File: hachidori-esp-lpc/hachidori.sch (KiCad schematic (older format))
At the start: 53 parts, among them P1 VIN, P2 UART, P3 ADC, P4 I2C, SW1 FLASH, SW2 RESET, U1 NCP1117ST33, U2 MPU-9250, U3 ESP-13-WROOM-02, U4 BME280, U7 INA226

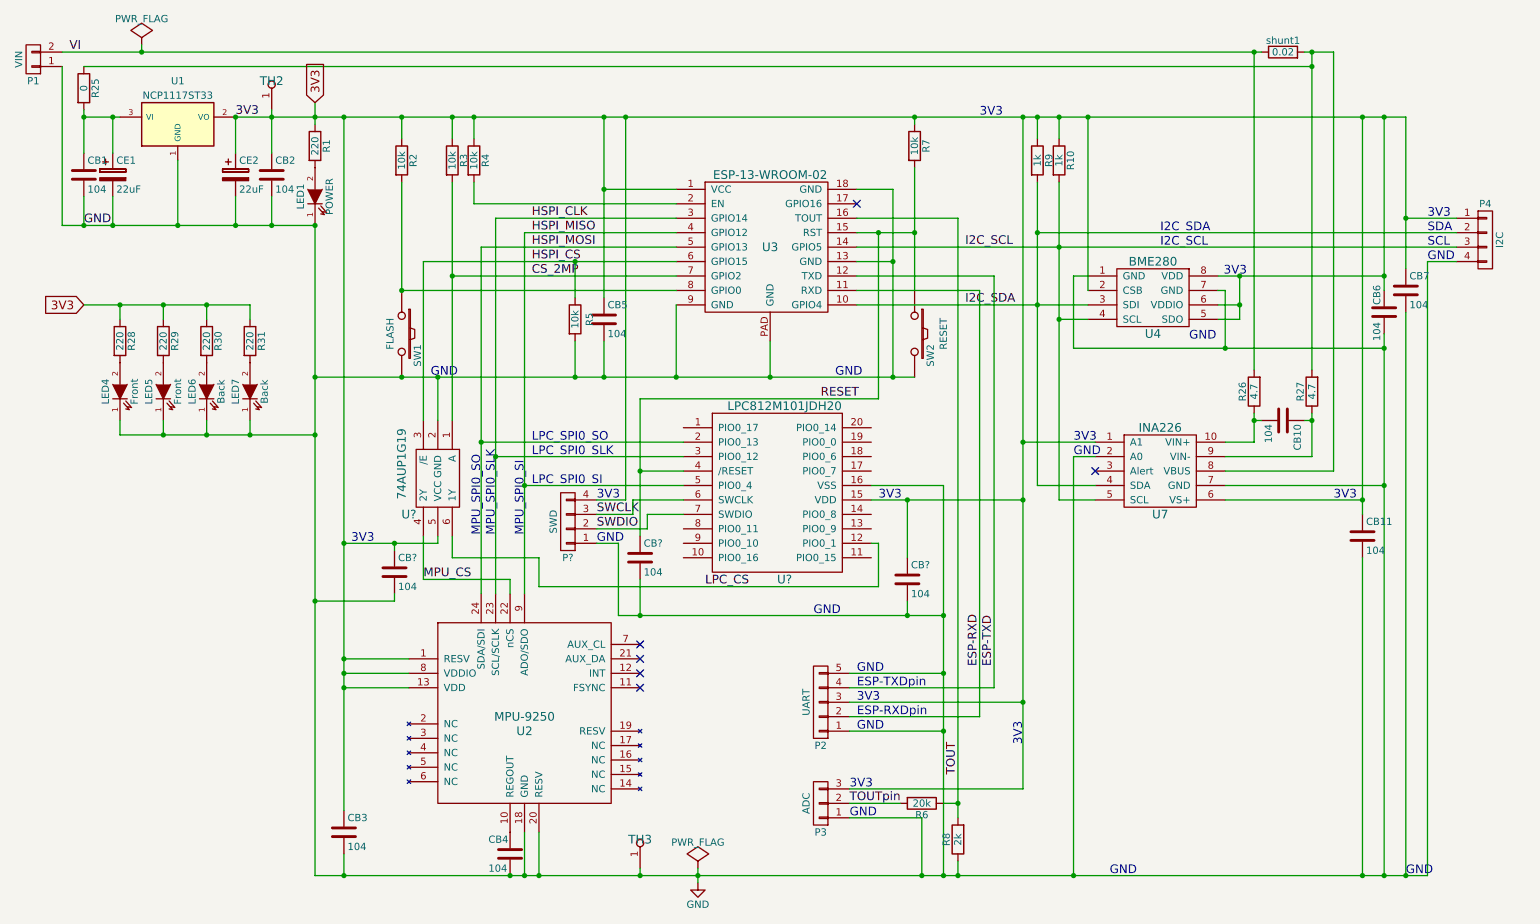
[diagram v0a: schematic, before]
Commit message: fix I2C interface
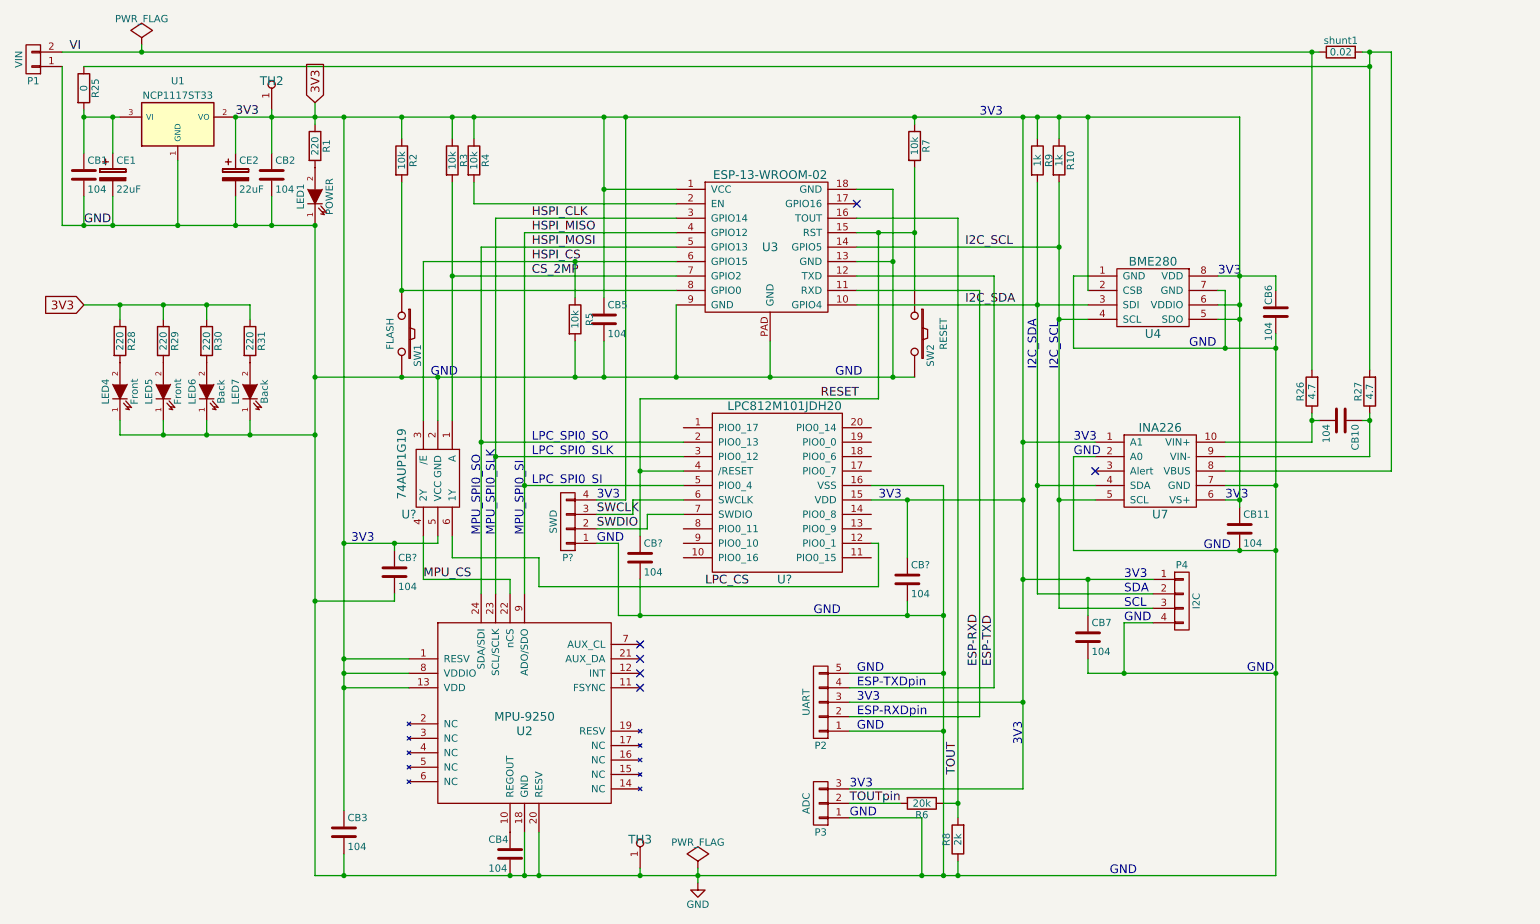
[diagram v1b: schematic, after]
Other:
- moved on the sheet: CB10, CB11, CB6, CB7, P4, R26, R27, shunt1

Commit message: fix interface positions
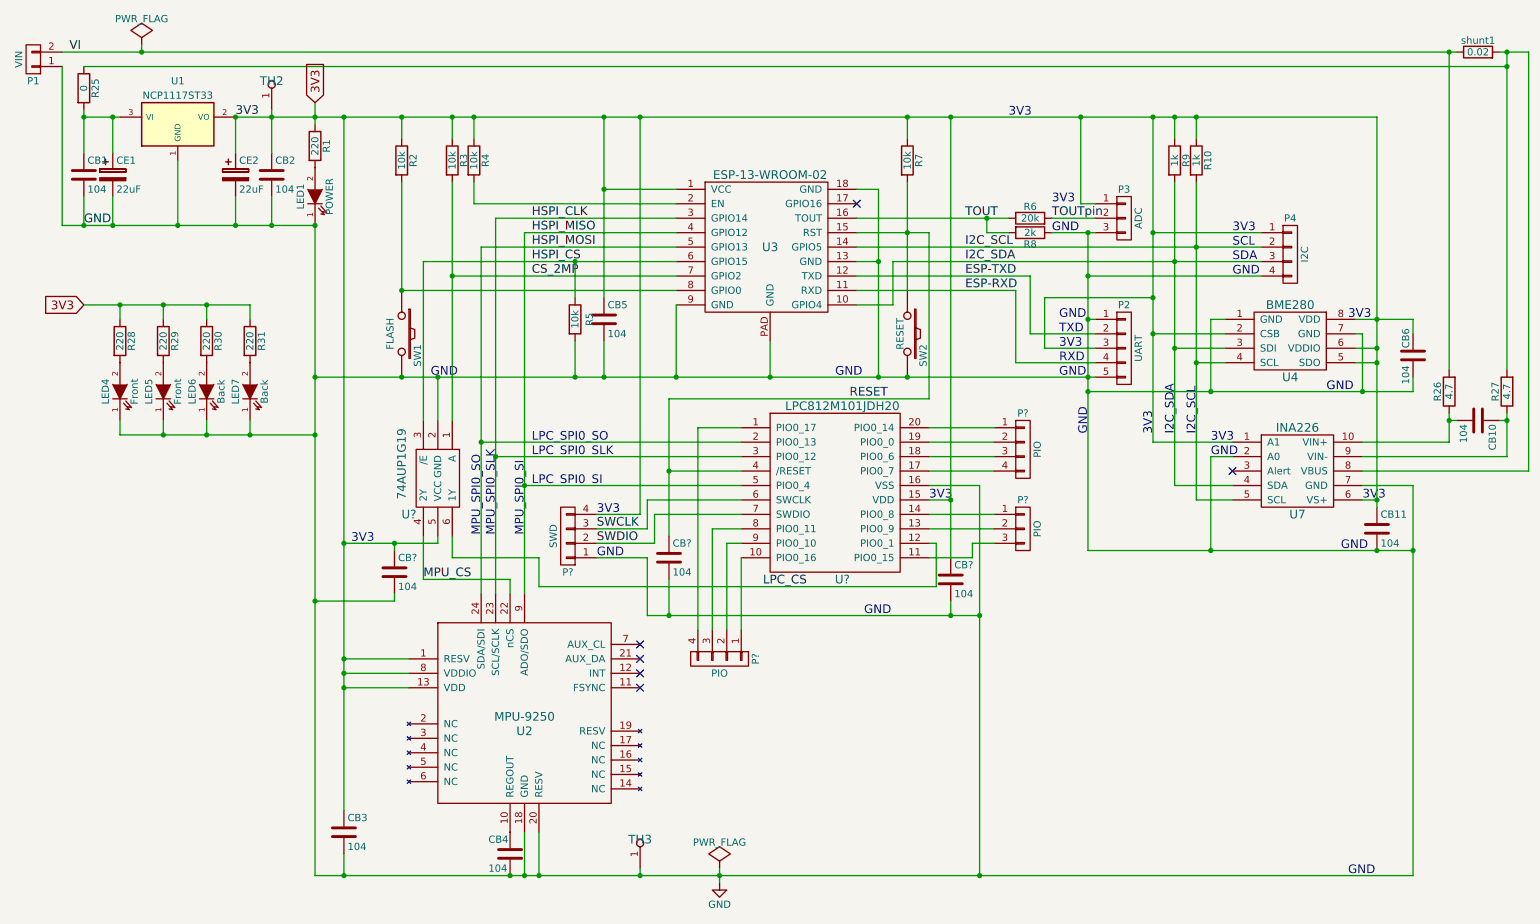
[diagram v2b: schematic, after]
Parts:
- removed CB7: 104, droneworks:GRM18, symbol C
- added P? (x2): PIO, symbol CONN_01X04
- added P?: PIO, droneworks:Pin_Header_1x03, symbol CONN_01X03
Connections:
- net 3V3: now also P3.1 (P1); no longer P3.3 (P3)
- net ESP-RXD: now also P2.4 (P4); no longer P2.2 (P2)
- net ESP-TXD: now also P2.2 (P2); no longer P2.4 (P4)
- net GND: now also P3.3 (P3); no longer P3.1 (P1)
- net I2C_SCL: now also P4.2 (P2); no longer P4.3 (P3)
- net I2C_SDA: now also P4.3 (P3); no longer P4.2 (P2)
- net at U?.1 (PIO0_17): now also P?.4 (P4)
- net at U?.10 (PIO0_16): now also P?.1 (P1)
- net at U?.11 (PIO0_15): now also P?.3 (P3)
- net at U?.13 (PIO0_9): now also P?.2 (P2)
- net at U?.14 (PIO0_8): now also P?.1 (P1)
- net at U?.17 (PIO0_7): now also P?.4 (P4)
- net at U?.18 (PIO0_6): now also P?.3 (P3)
- net at U?.19 (PIO0_0): now also P?.2 (P2)
- net at U?.20 (PIO0_14): now also P?.1 (P1)
- net at U?.8 (PIO0_11): now also P?.3 (P3)
- net at U?.9 (PIO0_10): now also P?.2 (P2)
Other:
- note added: "RXD"
- note added: "TXD"
- note removed: "ESP-RXDpin"
- note removed: "ESP-TXDpin"
- moved on the sheet: CB10, CB11, CB6, CB?, P2, P3, P4, P?, R10, R26, R27, R6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
